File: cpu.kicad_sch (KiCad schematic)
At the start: 47 parts, among them IC11 LM2936-3.0_TO92, IC12 LM2936-3.0, J11 Conn_01x03, J12 Conn_01x06_Female, J13 Conn_01x09_Female, J14 Conn_01x04_Male, J15 Conn_01x05_Male, J16 Conn_01x06_Female, J17 Conn_01x08_Female, Q11 DTC114E

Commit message: qrp-fm試作の反映
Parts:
- added J18: USB_C_POW, UserLib:USB_C_POW, symbol User_Library:USB_C_POW
- added S4: NM, UserLib:Switch_2P, symbol Switch:SW_Push
- C15: value 10u -> 100u; footprint Capacitor_THT:CP_Radial_Tantal_D7.0mm_P2.50mm -> Capacitor_THT:CP_Radial_D7.5mm_P2.50mm
- C18: value 0.1u -> 1000p
- D12: value LED -> LED-G
- D14: value LED -> LED-Y
- D16: value LED -> LED-R
- Q11: value DTC114E -> NM(DTC114E)
- R13: value 1k -> 10k
- R14, R17, R25: value 0 -> NM
- R15, R16, R27: value 1k -> NM
- R19: value 1k -> 2.2k
- R21: value 120k -> 100k
- R22: value 24k -> 22k
- R24: value 1k -> 4.7k
- R26: value 100 -> 10k
- S3: value SW_Push -> NM
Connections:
- net +3.3V-REG: now also IC11.3 (VO); no longer IC11.1 (VO)
- net +5VIN: now also IC11.1 (VI); no longer IC11.3 (VI)
- net GND: now also J18.2 (GND), S4.2
- net M5_EN: now also S4.1
- net at J11.2 (Pin_2), S1.1 (A), S1.2 (B): now also J18.1 (VBUS)
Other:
- note added: "AE-BME280"
- note added: "Add Ver2022.3"
- note added: "M5"
- note added: "M5 ATOM"
- note added: "M5 DL kit"
- note added: "M5 Stamp Pico"
- note added: "N.C."
- note added: "TRCV"

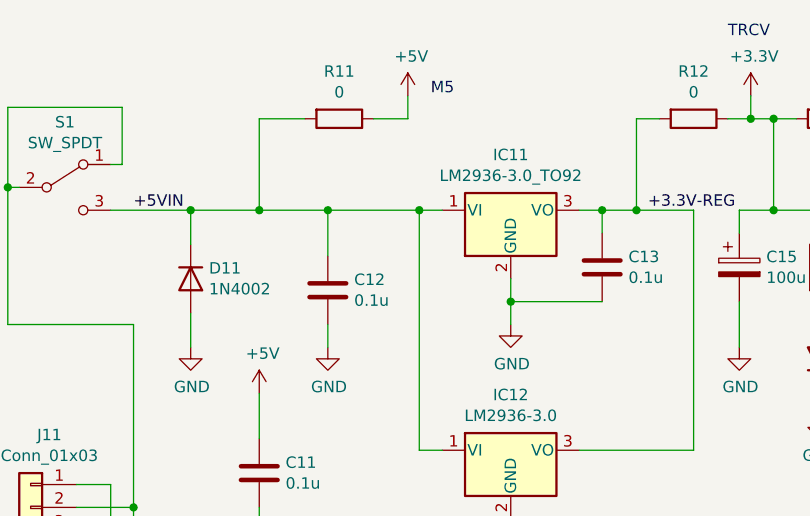
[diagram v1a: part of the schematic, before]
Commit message: Add files via upload
秋月の通販コード追加
部品表の代わりにxmlファイルを追加
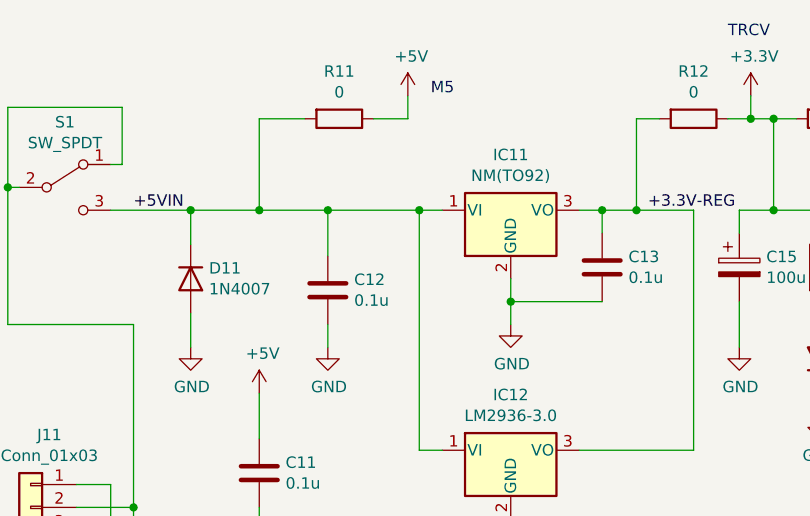
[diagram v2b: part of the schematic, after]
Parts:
- D11: value 1N4002 -> 1N4007
- IC11: value LM2936-3.0_TO92 -> NM(TO92)
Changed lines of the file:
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@@
       (effects (font (size 1.27 1.27)) hide)
     )
-    (property "Datasheet" "http://www.ti.com/lit/ds/symlink/lm2936.pdf" (id 3) (at 72.39 63.5 0)
+    (property "Datasheet" "I-02252" (id 3) (at 72.39 63.5 0)
       (effects (font (size 1.27 1.27)) hide)
     )
@@
     (in_bom yes) (on_board yes)
     (property "Reference" "IC11" (id 0) (at 72.39 29.4132 0))
-    (property "Value" "LM2936-3.0_TO92" (id 1) (at 72.39 31.7246 0))
+    (property "Value" "NM(TO92)" (id 1) (at 72.39 31.7246 0))
     (property "Footprint" "Package_TO_SOT_THT:TO-92_Inline_Wide" (id 2) (at 72.39 29.845 0)
       (effects (font (size 1.27 1.27) italic) hide)
     )
-    (property "Datasheet" "http://www.ti.com/lit/ds/symlink/lm2936.pdf" (id 3) (at 72.39 36.83 0)
+    (property "Datasheet" "~" (id 3) (at 72.39 36.83 0)
       (effects (font (size 1.27 1.27)) hide)
     )
@@
       (effects (font (size 1.27 1.27)) hide)
     )
-    (property "Datasheet" "~" (id 3) (at 52.07 44.45 0)
+    (property "Datasheet" "P-13582" (id 3) (at 52.07 44.45 0)
       (effects (font (size 1.27 1.27)) hide)
     )
@@
       (effects (font (size 1.27 1.27)) hide)
     )
-    (property "Datasheet" "~" (id 3) (at 118.11 41.91 0)
+    (property "Datasheet" "P-13582" (id 3) (at 118.11 41.91 0)
       (effects (font (size 1.27 1.27)) hide)
     )
@@
       (effects (font (size 1.27 1.27)) hide)
     )
-    (property "Datasheet" "~" (id 3) (at 190.5 140.97 0)
+    (property "Datasheet" "I-11577" (id 3) (at 190.5 140.97 0)
       (effects (font (size 1.27 1.27)) hide)
     )
@@
       (effects (font (size 1.27 1.27)) hide)
     )
-    (property "Datasheet" "~" (id 3) (at 82.55 41.91 0)
+    (property "Datasheet" "P-13582" (id 3) (at 82.55 41.91 0)
       (effects (font (size 1.27 1.27)) hide)
     )
@@
       (effects (font (size 1.27 1.27)) hide)
     )
-    (property "Datasheet" "~" (id 3) (at 106.68 52.07 0)
+    (property "Datasheet" "I-11635" (id 3) (at 106.68 52.07 0)
       (effects (font (size 1.27 1.27)) hide)
     )
@@
       (effects (font (size 1.27 1.27)) (justify left))
     )
-    (property "Value" "1N4002" (id 1) (at 38.862 44.323 90)
+    (property "Value" "1N4007" (id 1) (at 38.862 44.323 90)
       (effects (font (size 1.27 1.27)) (justify left))
     )
@@
       (effects (font (size 1.27 1.27)) hide)
     )
-    (property "Datasheet" "http://www.vishay.com/docs/88503/1n4001.pdf" (id 3) (at 36.83 43.18 0)
+    (property "Datasheet" "I-08332" (id 3) (at 36.83 43.18 0)
       (effects (font (size 1.27 1.27)) hide)
     )
@@
       (effects (font (size 1.27 1.27)) hide)
     )
-    (property "Datasheet" "~" (id 3) (at 19.05 68.58 0)
+    (property "Datasheet" "C-00167" (id 3) (at 19.05 68.58 0)
       (effects (font (size 1.27 1.27)) hide)
     )
@@
       (effects (font (size 1.27 1.27)) hide)
     )
-    (property "Datasheet" "~" (id 3) (at 44.45 64.77 0)
+    (property "Datasheet" "P-13582" (id 3) (at 44.45 64.77 0)
       (effects (font (size 1.27 1.27)) hide)
     )
@@
       (effects (font (size 1.27 1.27)) hide)
     )
-    (property "Datasheet" "~" (id 3) (at 233.68 134.62 0)
+    (property "Datasheet" "C-00167" (id 3) (at 233.68 134.62 0)
       (effects (font (size 1.27 1.27)) hide)
     )
@@
       (effects (font (size 1.27 1.27)) hide)
     )
-    (property "Datasheet" "~" (id 3) (at 241.3 134.62 0)
+    (property "Datasheet" "C-00167" (id 3) (at 241.3 134.62 0)
       (effects (font (size 1.27 1.27)) hide)
     )
@@
       (effects (font (size 1.27 1.27)) hide)
     )
-    (property "Datasheet" "~" (id 3) (at 180.34 74.93 0)
+    (property "Datasheet" "C-03138" (id 3) (at 180.34 74.93 0)
       (effects (font (size 1.27 1.27)) hide)
     )
@@
       (effects (font (size 1.27 1.27)) hide)
     )
-    (property "Datasheet" "~" (id 3) (at 194.31 77.47 0)
+    (property "Datasheet" "C-05779" (id 3) (at 194.31 77.47 0)
       (effects (font (size 1.27 1.27)) hide)
     )
@@
       (effects (font (size 1.27 1.27)) hide)
     )
-    (property "Datasheet" "~" (id 3) (at 227.33 74.93 0)
+    (property "Datasheet" "C-05779" (id 3) (at 227.33 74.93 0)
       (effects (font (size 1.27 1.27)) hide)
     )
@@
       (effects (font (size 1.27 1.27)) hide)
     )
-    (property "Datasheet" "~" (id 3) (at 111.76 83.82 0)
+    (property "Datasheet" "R-25000" (id 3) (at 111.76 83.82 0)
       (effects (font (size 1.27 1.27)) hide)
     )
@@
       (effects (font (size 1.27 1.27)) (justify left) hide)
     )
-    (property "Datasheet" "" (id 3) (at 200.66 124.46 0)
+    (property "Datasheet" "I-16747" (id 3) (at 200.66 124.46 0)
       (effects (font (size 1.27 1.27)) (justify left) hide)
     )
@@
       (effects (font (size 1.27 1.27)) hide)
     )
-    (property "Datasheet" "http://www.vishay.com/docs/88503/1n4001.pdf" (id 3) (at 156.21 36.83 0)
+    (property "Datasheet" "I-07783" (id 3) (at 156.21 36.83 0)
       (effects (font (size 1.27 1.27)) hide)
     )
@@
       (effects (font (size 1.27 1.27)) hide)
     )
-    (property "Datasheet" "http://www.vishay.com/docs/88503/1n4001.pdf" (id 3) (at 151.13 26.67 0)
+    (property "Datasheet" "I-07783" (id 3) (at 151.13 26.67 0)
       (effects (font (size 1.27 1.27)) hide)
     )
@@
       (effects (font (size 1.27 1.27)) hide)
     )
-    (property "Datasheet" "~" (id 3) (at 223.52 38.1 0)
+    (property "Datasheet" "P-04062" (id 3) (at 223.52 38.1 0)
       (effects (font (size 1.27 1.27)) hide)
     )
@@
       (effects (font (size 1.27 1.27)) hide)
     )
-    (property "Datasheet" "~" (id 3) (at 240.03 38.1 0)
+    (property "Datasheet" "P-14902" (id 3) (at 240.03 38.1 0)
       (effects (font (size 1.27 1.27)) hide)
     )
@@
       (effects (font (size 1.27 1.27)) hide)
     )
-    (property "Datasheet" "~" (id 3) (at 254 38.1 0)
+    (property "Datasheet" "P-13582" (id 3) (at 254 38.1 0)
       (effects (font (size 1.27 1.27)) hide)
     )
@@
       (effects (font (size 1.27 1.27)) hide)
     )
-    (property "Datasheet" "~" (id 3) (at 177.8 36.83 0)
+    (property "Datasheet" "P-13582" (id 3) (at 177.8 36.83 0)
       (effects (font (size 1.27 1.27)) hide)
     )
@@
       (effects (font (size 1.27 1.27)) hide)
     )
-    (property "Datasheet" "~" (id 3) (at 157.48 88.9 0)
+    (property "Datasheet" "P-13582" (id 3) (at 157.48 88.9 0)
       (effects (font (size 1.27 1.27)) hide)
     )
@@
       (effects (font (size 1.27 1.27)) hide)
     )
-    (property "Datasheet" "~" (id 3) (at 201.93 54.61 0)
+    (property "Datasheet" "R-25000" (id 3) (at 201.93 54.61 0)
       (effects (font (size 1.27 1.27)) hide)
     )
@@
       (effects (font (size 1.27 1.27)) hide)
     )
-    (property "Datasheet" "~" (id 3) (at 92.71 25.4 0)
+    (property "Datasheet" "R-25000" (id 3) (at 92.71 25.4 0)
       (effects (font (size 1.27 1.27)) hide)
     )
@@
       (effects (font (size 1.27 1.27)) hide)
     )
-    (property "Datasheet" "~" (id 3) (at 53.34 25.4 0)
+    (property "Datasheet" "R-25000" (id 3) (at 53.34 25.4 0)
       (effects (font (size 1.27 1.27)) hide)
     )
@@
       (effects (font (size 1.27 1.27)) hide)
     )
-    (property "Datasheet" "~" (id 3) (at 143.51 128.27 0)
+    (property "Datasheet" "I-11639" (id 3) (at 143.51 128.27 0)
       (effects (font (size 1.27 1.27)) hide)
     )
@@
       (effects (font (size 1.27 1.27)) hide)
     )
-    (property "Datasheet" "~" (id 3) (at 93.98 106.68 0)
+    (property "Datasheet" "C-03138" (id 3) (at 93.98 106.68 0)
       (effects (font (size 1.27 1.27)) hide)
     )
@@
       (effects (font (size 1.27 1.27)) hide)
     )
-    (property "Datasheet" "~" (id 3) (at 133.35 114.3 0)
+    (property "Datasheet" "R-25000" (id 3) (at 133.35 114.3 0)
       (effects (font (size 1.27 1.27)) hide)
     )
@@
       (effects (font (size 1.27 1.27)) hide)
     )
-    (property "Datasheet" "~" (id 3) (at 101.6 90.17 0)
-      (effects (font (size 1.27 1.27)) hide)
-    )
+    (property "Datasheet" "P-13582" (id 3) (at 101.6 90.17 0)
+      (effects (font (size 1.27 1.27)) hide)
+    )

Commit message: バンドパスフィルタ見直し
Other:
- company: (none) -> PRUG
- title: (none) -> QRP-TNC
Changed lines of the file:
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@@
 (kicad_sch (version 20211123) (generator eeschema)
   (paper "A4")
+  (title_block
+    (title "QRP-TNC")
+    (date "2022-05-03")
+    (company "PRUG")
+  )
   (junction (at 152.4 77.47) (diameter 0) (color 0 0 0 0)
   )
